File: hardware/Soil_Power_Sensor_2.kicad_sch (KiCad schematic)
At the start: 19 parts, among them J9 Conn_01x03_Pin, U5 REF2033, U8 TPS60400DBV

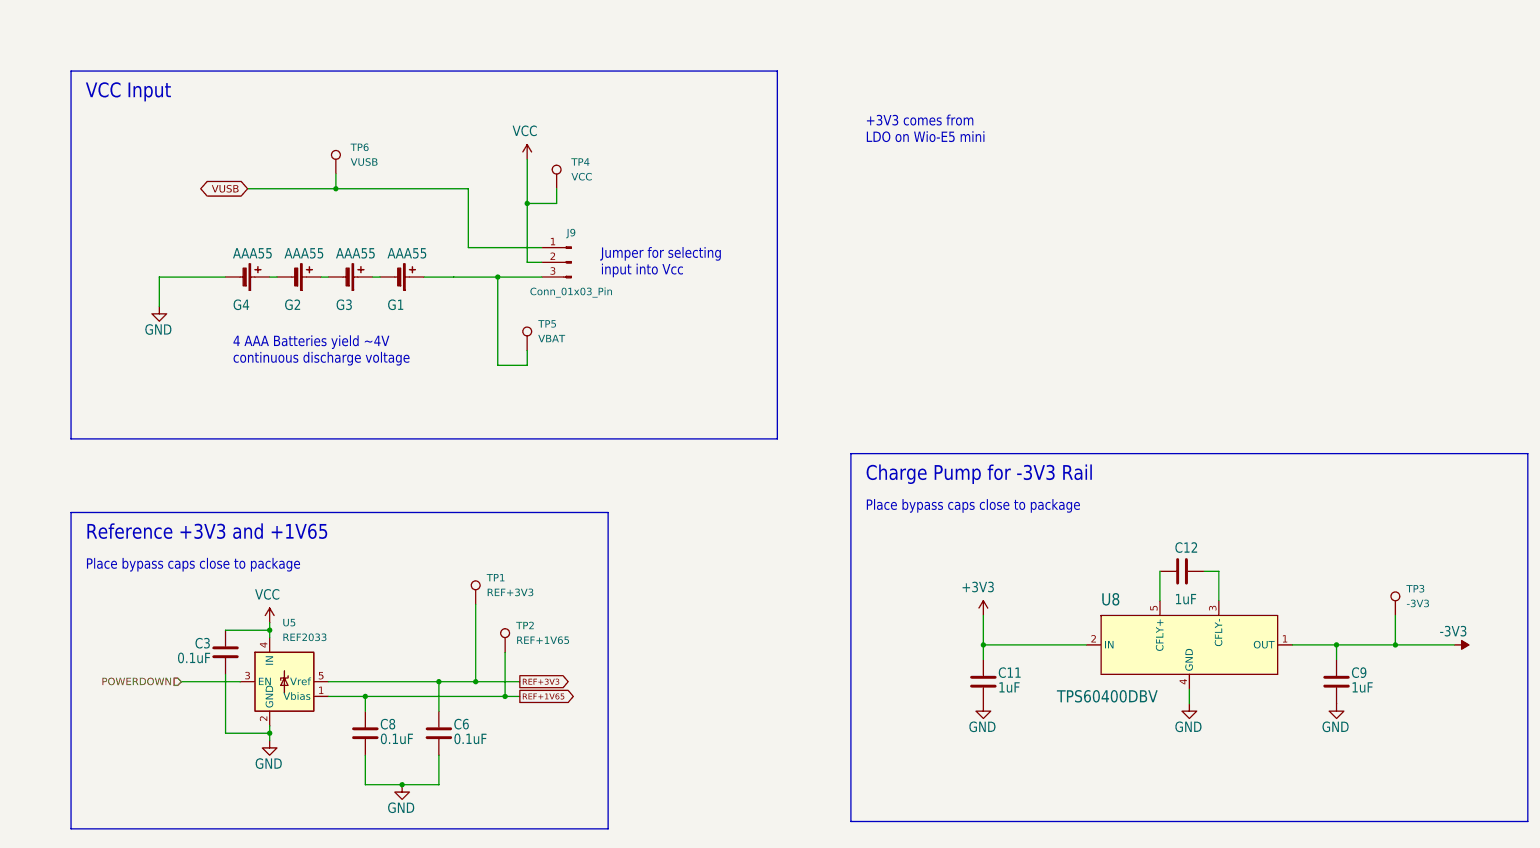
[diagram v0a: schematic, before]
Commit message: Added solder point for Vcc
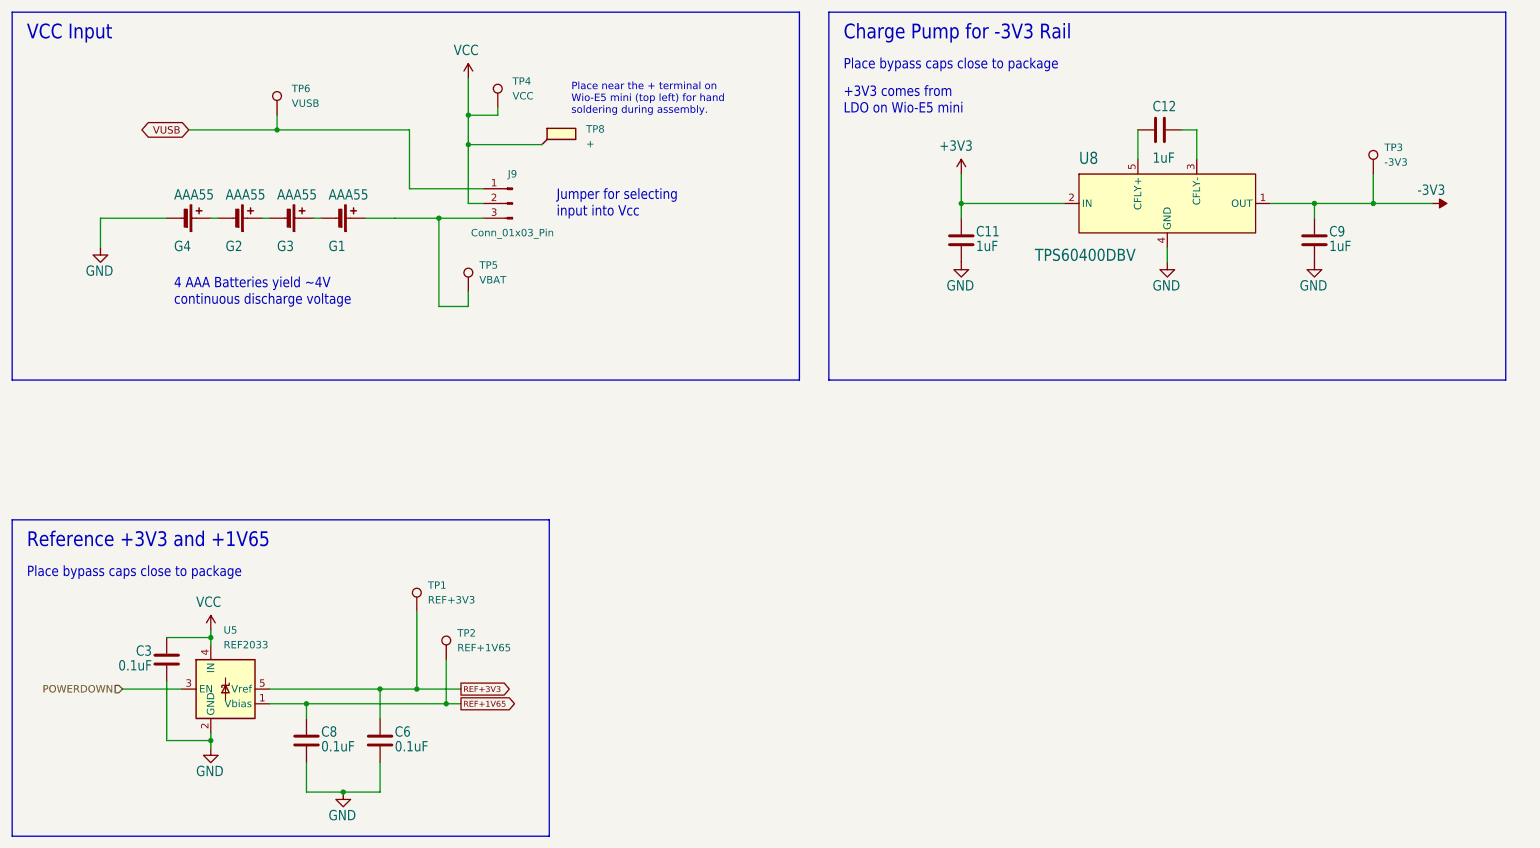
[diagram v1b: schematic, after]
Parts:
- added TP8: +, symbol Connector:TestPoint_Flag
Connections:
- net VCC: now also TP8.1
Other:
- note added: "Place near the + terminal on Wio-E5 mini (top left) for hand soldering during assembly."
- moved on the sheet: C11, C12, C3, C6, C8, C9, G1, G2, G3, G4, J9, TP1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

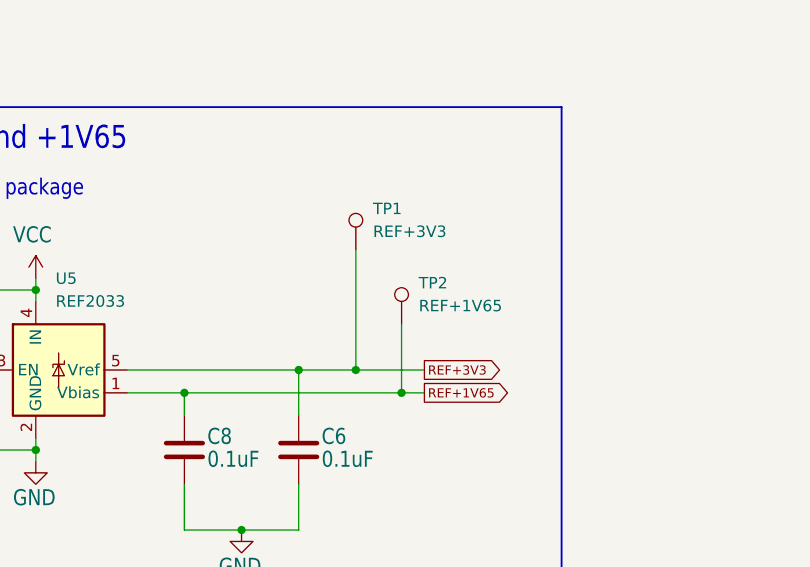
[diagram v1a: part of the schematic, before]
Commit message: Fixed ERC errors
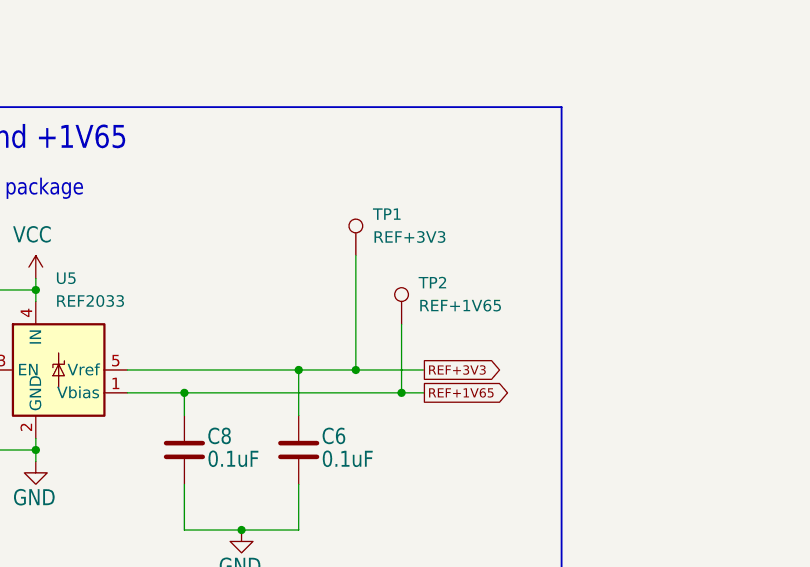
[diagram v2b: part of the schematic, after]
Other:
- moved on the sheet: TP1
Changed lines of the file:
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@@
     (stroke (width 0.1524) (type solid))
   )
-  (wire (pts (xy 90.17 123.825) (xy 90.17 137.16))
+  (wire (pts (xy 90.17 124.46) (xy 90.17 137.16))
     (stroke (width 0.1524) (type solid))
   )
@@
     )
   )
-  (symbol (lib_id "Connector:TestPoint") (at 90.17 123.825 0) (unit 1)
+  (symbol (lib_id "Connector:TestPoint") (at 90.17 124.46 0) (unit 1)
     (in_bom yes) (on_board yes) (dnp no) (fields_autoplaced)
-    (property "Reference" "TP1" (at 92.075 119.253 0)
-      (effects (font (size 1.27 1.27)) (justify left))
-    )
-    (property "Value" "REF+3V3" (at 92.075 121.793 0)
-      (effects (font (size 1.27 1.27)) (justify left))
-    )
-    (property "Footprint" "TestPoint:TestPoint_Pad_D1.5mm" (at 95.25 123.825 0)
-      (effects (font (size 1.27 1.27)) hide)
-    )
-    (property "Datasheet" "~" (at 95.25 123.825 0)
-      (effects (font (size 1.27 1.27)) hide)
-    )
+    (property "Reference" "TP1" (at 92.075 119.888 0)
+      (effects (font (size 1.27 1.27)) (justify left))
+    )
+    (property "Value" "REF+3V3" (at 92.075 122.428 0)
+      (effects (font (size 1.27 1.27)) (justify left))
+    )
+    (property "Footprint" "TestPoint:TestPoint_Pad_D1.5mm" (at 95.25 124.46 0)
+      (effects (font (size 1.27 1.27)) hide)
+    )
+    (property "Datasheet" "~" (at 95.25 124.46 0)
+      (effects (font (size 1.27 1.27)) hide)
+    )

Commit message: Updated board layout
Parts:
- TP8: footprint (none) -> TestPoint:TestPoint_Pad_2.0x2.0mm
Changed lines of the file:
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@@
       (effects (font (size 1.27 1.27)) (justify left))
     )
-    (property "Footprint" "" (at 116.84 43.18 0)
+    (property "Footprint" "TestPoint:TestPoint_Pad_2.0x2.0mm" (at 116.84 43.18 0)
       (effects (font (size 1.27 1.27)) hide)
     )
